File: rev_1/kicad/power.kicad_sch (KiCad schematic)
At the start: 54 parts, among them J4 TYPE-C-31-M-12, U10 MC34063AD, U11 MC34063AD, U12 XC6206P332MR-G, U13 TPS2116DRLR

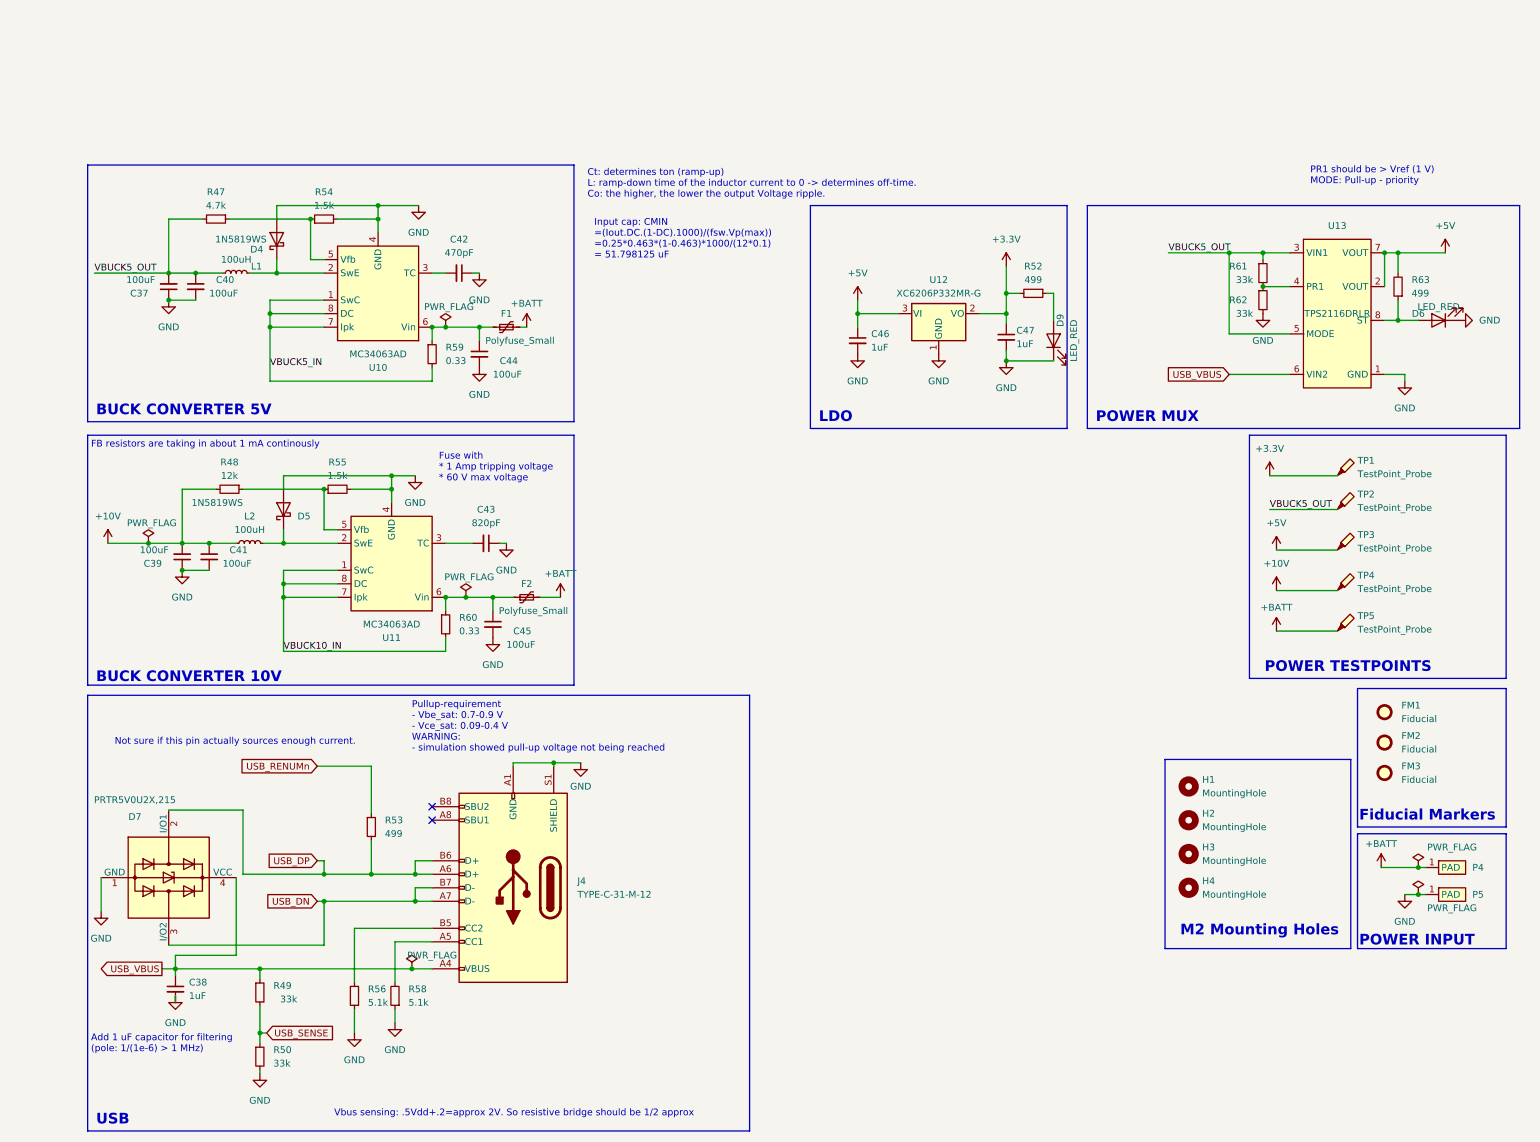
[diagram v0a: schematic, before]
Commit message: [kicad] (minor) Added comments about bldc strategy
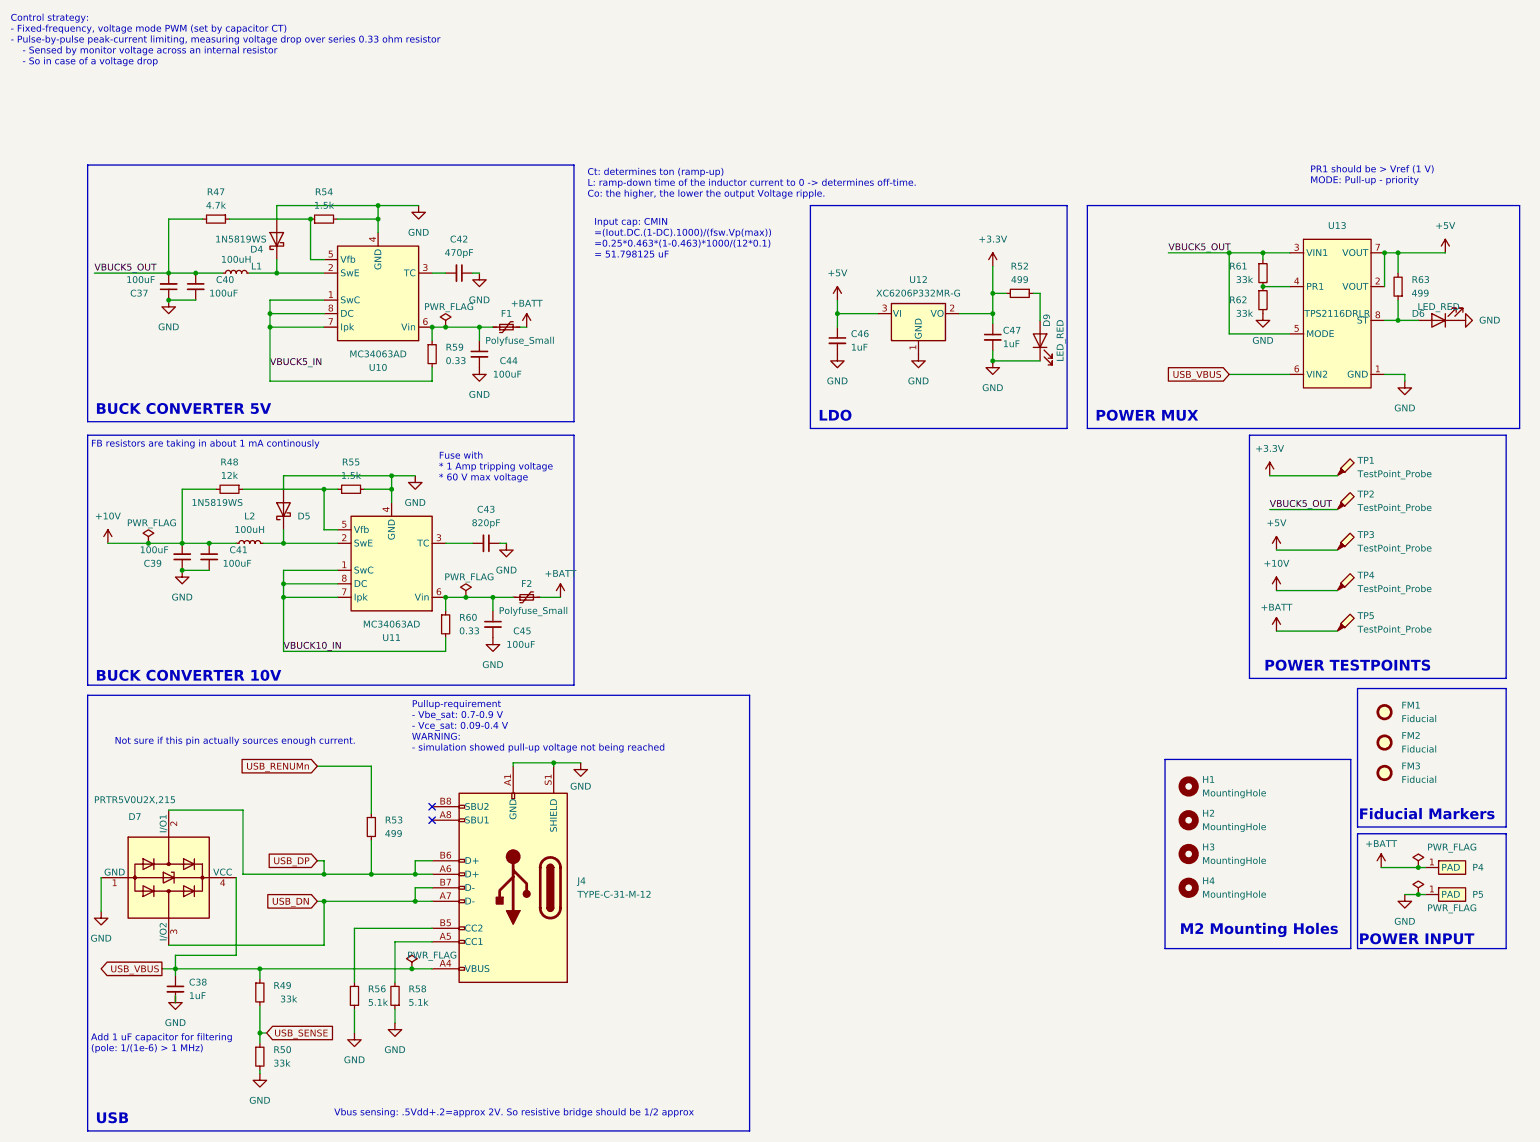
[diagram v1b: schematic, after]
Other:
- note added: "Control strategy: - Fixed-frequency, voltage mode PWM (set by capacitor CT) - Pulse-by-pulse peak-current limiting, measuring voltage drop over series 0.33 ohm resistor - Sensed by monitor voltage across an internal resistor - So in case of a voltage drop"
- moved on the sheet: C46, C47, D9, R52, R55, U12
